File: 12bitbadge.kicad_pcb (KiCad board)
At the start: 2 copper layers, 62.6 x 53.7 mm, 44 parts, among them J1 Conn_02x04_Counter_Clockwise, J2 Conn_02x04_Counter_Clockwise, J3 Conn_02x04_Counter_Clockwise, J4 Conn_02x03_Odd_Even, J5 Conn_02x03_Odd_Even, J6 Conn_02x03_Odd_Even, J7 Conn_02x03_Odd_Even, SW1 SW_SPDT, SW10 SW_SPDT, SW11 SW_SPDT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

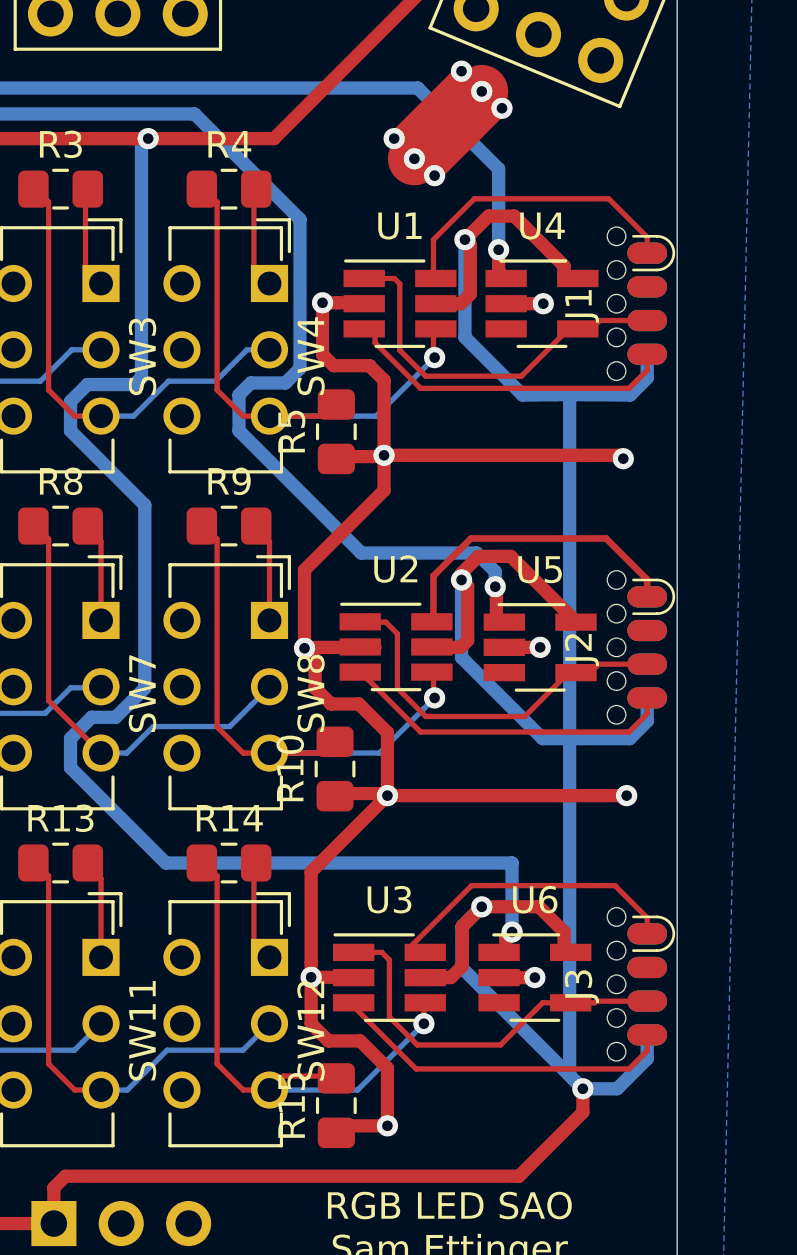
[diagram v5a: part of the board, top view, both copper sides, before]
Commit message: Replaced switches with PWM-friendly MOSFETs
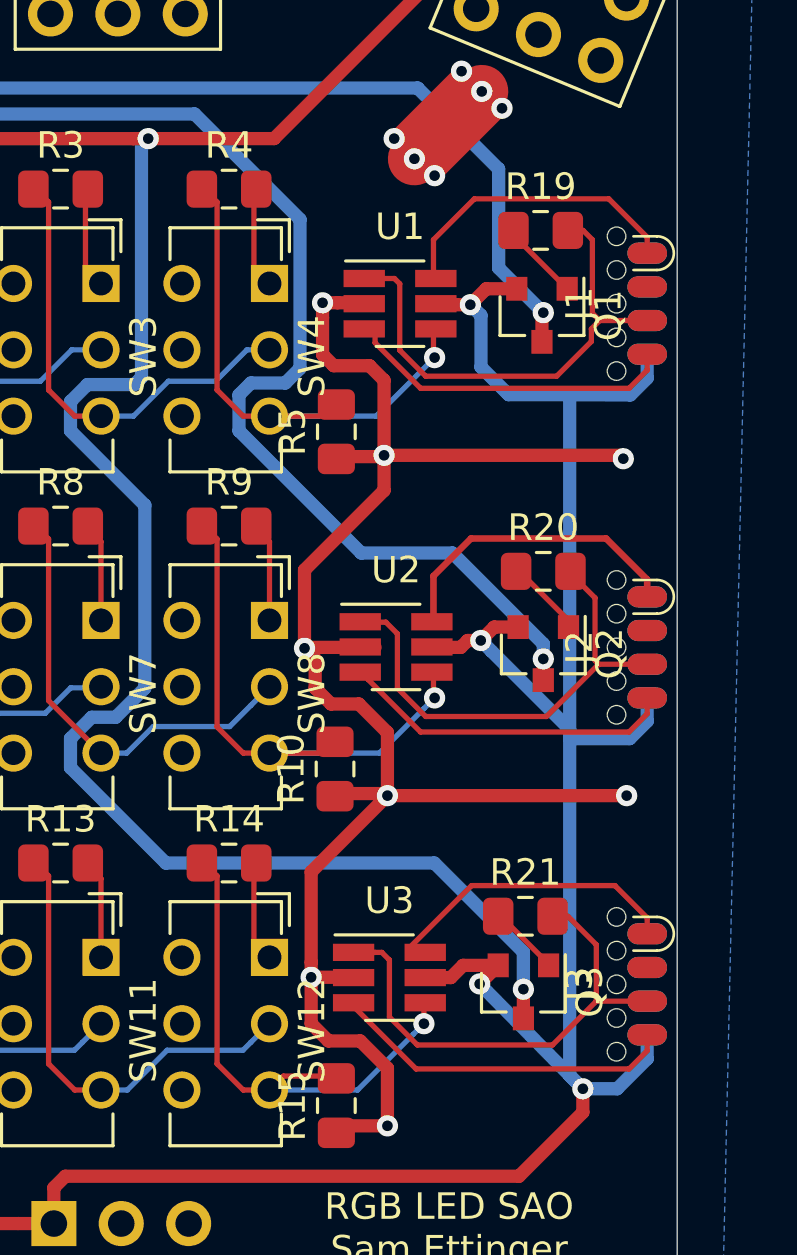
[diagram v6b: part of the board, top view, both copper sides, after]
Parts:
- removed U4, U5, U6: TPS2041B, Package_TO_SOT_SMD:SOT-23-5_HandSoldering
- added Q1: Q_PMOS_GSD, Package_TO_SOT_SMD:SOT-23, F.Cu at (186.8, 52.0)
- added Q2: Q_PMOS_GSD, Package_TO_SOT_SMD:SOT-23, F.Cu at (186.8, 64.8)
- added Q3: Q_PMOS_GSD, Package_TO_SOT_SMD:SOT-23, F.Cu at (186.1, 77.5)
- added R19: 1k, Resistor_SMD:R_0805_2012Metric_Pad1.15x1.40mm_HandSolder, F.Cu at (186.8, 48.8)
- added R20: 1k, Resistor_SMD:R_0805_2012Metric_Pad1.15x1.40mm_HandSolder, F.Cu at (186.8, 61.6)
- added R21: 1k, Resistor_SMD:R_0805_2012Metric_Pad1.15x1.40mm_HandSolder, F.Cu at (186.2, 74.7)
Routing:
- net 3.3V: track 176.0 -> 150.9 mm
- net G_OUT: track 13.2 -> 17.7 mm
- net B_OUT: track 14.1 -> 18.3 mm
- net R_OUT: track 14.7 -> 18.7 mm
- net 0V: track 81.9 -> 78.3 mm, vias 17 -> 14
- net Net-(Q1-Pad1): track 0.00 -> 3.04 mm
- net Net-(Q2-Pad1): track 0.00 -> 2.99 mm
- net PWR_OUT_1: track 62.7 -> 65.5 mm
- net Net-(Q3-Pad1): track 0.00 -> 2.70 mm
- net PWR_OUT_2: track 79.1 -> 81.4 mm
- net PWR_OUT_3: track 108.0 -> 108.8 mm

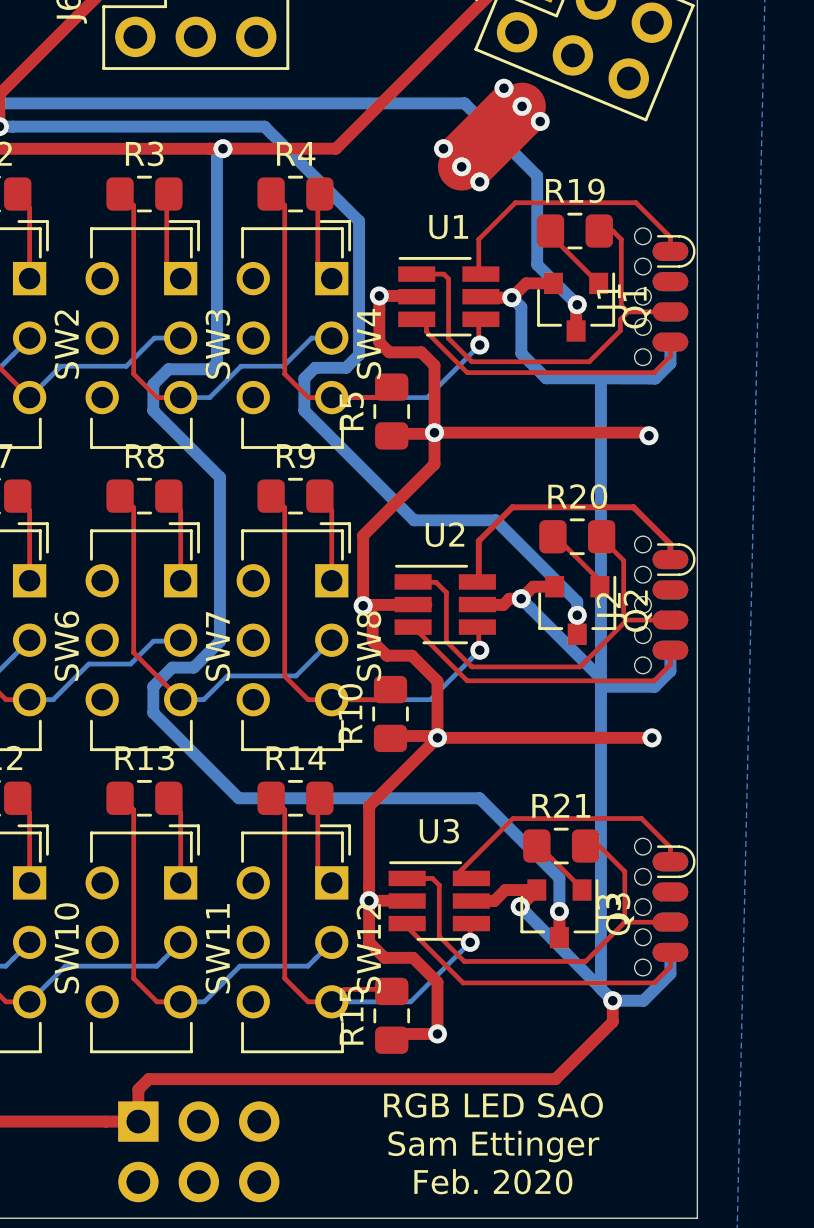
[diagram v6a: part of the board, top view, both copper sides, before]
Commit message: Updated MOSFETs to hand-solderable pads
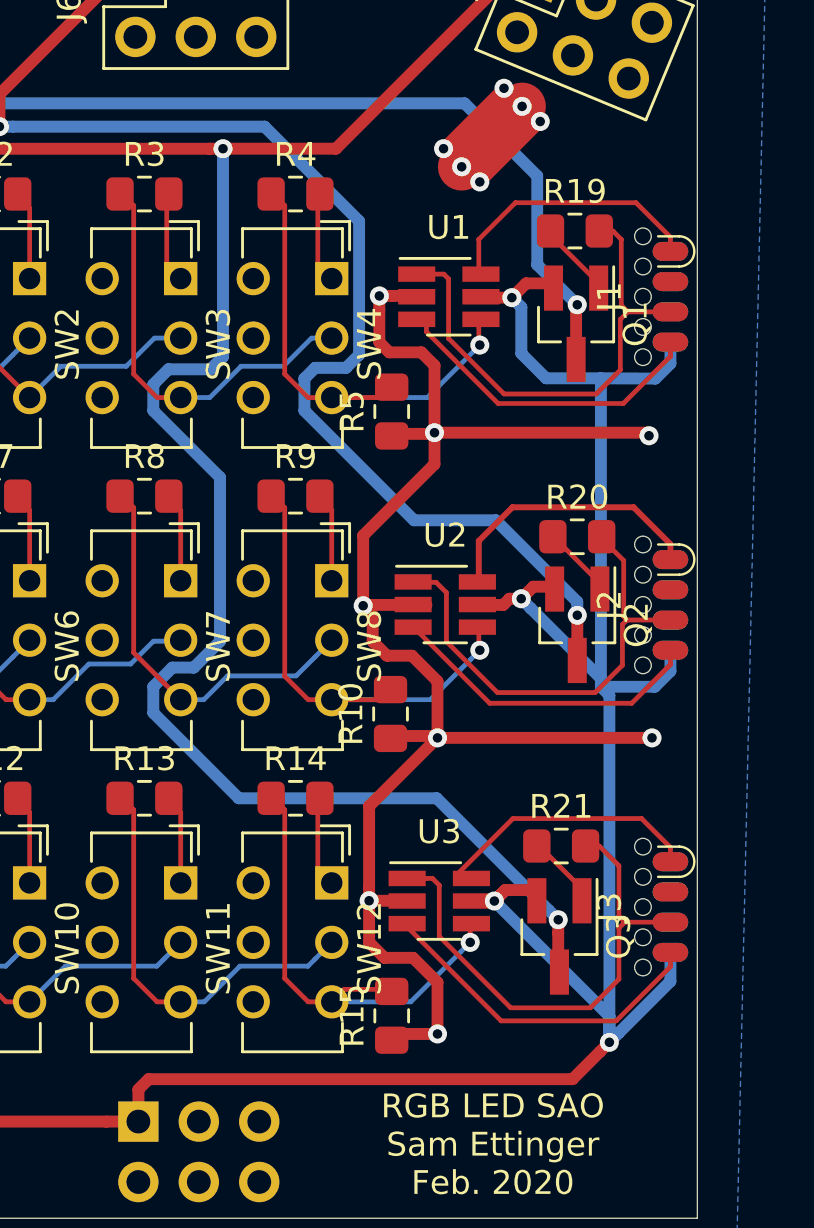
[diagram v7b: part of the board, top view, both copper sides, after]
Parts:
- Q1, Q2, Q3: footprint Package_TO_SOT_SMD:SOT-23 -> Package_TO_SOT_SMD:SOT-23_Handsoldering
- moved Q3 0.95 mm to (186.1, 78.5)
- moved Q1 0.70 mm to (186.8, 52.7)
- moved Q2 0.60 mm to (186.8, 65.3)
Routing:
- net 3.3V: track 150.9 -> 154.3 mm
- net B_OUT: track 18.3 -> 21.2 mm
- net R_OUT: track 18.7 -> 20.8 mm
- net G_OUT: track 17.7 -> 19.6 mm
- net /tpi_clk_3: track 13.1 -> 14.4 mm
- net PWR_OUT_1: track 65.5 -> 66.7 mm
- net PWR_OUT_2: track 81.4 -> 82.5 mm
- net /tpi_clk_1: track 12.4 -> 13.5 mm
- net /tpi_clk_2: track 12.6 -> 13.4 mm
